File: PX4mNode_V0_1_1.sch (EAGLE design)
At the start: 128 parts, among them J201 DF13C-6P-1.25V, J202 DF13C-6P-1.25V, J203 DF13C-6P-1.25V, J301 DF13C-4P-1.25V, J401 DF13C-7P-1.25V, J402 DF13-4P-1.25V, J403 DF13C-4P-1.25V, J404 DF13C-4P-1.25V, J405 DF13C-4P-1.25V, J801 DF13C-3P-1.25V, M3_MOUNT1101 MOUNT-HOLE3.1MM, M3_MOUNT1102 MOUNT-HOLE3.1MM, M3_MOUNT1103 MOUNT-HOLE3.1MM, M3_MOUNT1104 MOUNT-HOLE3.1MM, U101 STM32F4X7VX, U401 MAX3051, U402 MAX3051, X101 3.2x2.5 mm / 24 MHz / 15 ppm

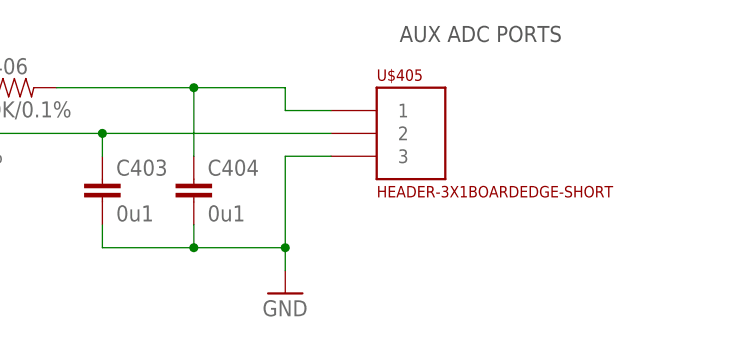
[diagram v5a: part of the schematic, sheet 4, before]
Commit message: Renamed and moved some component names
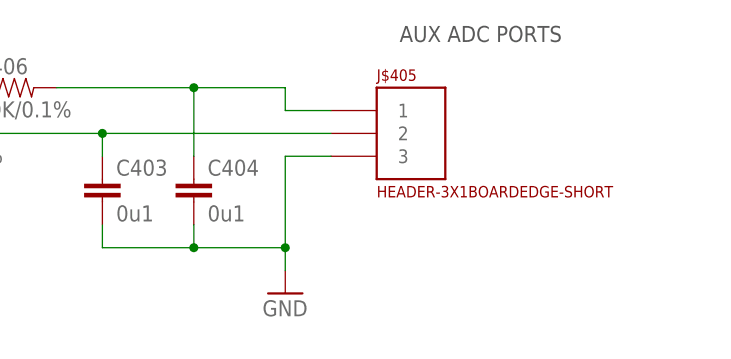
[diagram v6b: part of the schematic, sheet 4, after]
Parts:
- renumbered U$405 to J$405, U$601 to L$601
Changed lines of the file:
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@@
 <part name="L402" library="PX4lite" deviceset="NUF8402MN" device=""/>
 <part name="SJ403" library="SparkFun-Passives" deviceset="SOLDERJUMPER" device="TRACE"/>
-<part name="U$405" library="PX4lite" deviceset="HEADER-3X1" device="BOARDEDGE-SHORT"/>
+<part name="J$405" library="PX4lite" deviceset="HEADER-3X1" device="BOARDEDGE-SHORT"/>
 <part name="C403" library="pixhawk2" deviceset="CAP" device="0402" value="0u1">
 <attribute name="PARTNO" value="CC0402ZRY5V7BB104"/>
@@
 <part name="D903" library="SparkFun-DiscreteSemi" deviceset="DIODE" device="SMA" value="B340A"/>
 <part name="U$602" library="PX4lite" deviceset="TPS6303X" device=""/>
-<part name="U$601" library="ti_tps_soln2" deviceset="XFL4020-222MEB" device=""/>
+<part name="L$601" library="ti_tps_soln2" deviceset="XFL4020-222MEB" device=""/>
 <part name="SUPPLY2" library="supply2" deviceset="GND" device=""/>
 <part name="C607" library="SparkFun-Capacitors" deviceset="22UF-16V-20%-(1210)" device="" value="22uF"/>
@@
 <instance part="L402" gate="G$4" x="127" y="132.08"/>
 <instance part="SJ403" gate="1" x="205.74" y="58.42"/>
-<instance part="U$405" gate="G$1" x="228.6" y="157.48"/>
+<instance part="J$405" gate="G$1" x="228.6" y="157.48"/>
 <instance part="C403" gate="G$1" x="195.58" y="152.4">
 <attribute name="PARTNO" x="195.58" y="152.4" size="1.778" layer="96" display="off"/>
@@
 <wire x1="205.74" y1="165.1" x2="215.9" y2="165.1" width="0.1524" layer="91"/>
 <wire x1="215.9" y1="165.1" x2="215.9" y2="162.56" width="0.1524" layer="91"/>
-<pinref part="U$405" gate="G$1" pin="1"/>
+<pinref part="J$405" gate="G$1" pin="1"/>
 <wire x1="215.9" y1="162.56" x2="220.98" y2="162.56" width="0.1524" layer="91"/>
 <pinref part="C404" gate="G$1" pin="1"/>
@@
 <pinref part="R405" gate="G$1" pin="2"/>
 <wire x1="182.88" y1="160.02" x2="195.58" y2="160.02" width="0.1524" layer="91"/>
-<pinref part="U$405" gate="G$1" pin="2"/>
+<pinref part="J$405" gate="G$1" pin="2"/>
 <pinref part="C403" gate="G$1" pin="1"/>
 <wire x1="195.58" y1="160.02" x2="220.98" y2="160.02" width="0.1524" layer="91"/>
@@
 <wire x1="220.98" y1="157.48" x2="215.9" y2="157.48" width="0.1524" layer="91"/>
 <wire x1="215.9" y1="157.48" x2="215.9" y2="147.32" width="0.1524" layer="91"/>
-<pinref part="U$405" gate="G$1" pin="3"/>
+<pinref part="J$405" gate="G$1" pin="3"/>
 <pinref part="C403" gate="G$1" pin="2"/>
 <wire x1="215.9" y1="147.32" x2="215.9" y2="144.78" width="0.1524" layer="91"/>
@@
 <instance part="FRAME11" gate="G$1" x="0" y="0"/>
 <instance part="U$602" gate="A" x="101.6" y="109.22" smashed="yes"/>
-<instance part="U$601" gate="A" x="101.6" y="144.78" smashed="yes">
+<instance part="L$601" gate="A" x="101.6" y="144.78" smashed="yes">
 <attribute name="NAME" x="96.8756" y="149.4536" size="2.0828" layer="95" ratio="6" rot="SR0"/>
 <attribute name="VALUE" x="88.3158" y="141.1986" size="2.0828" layer="96" ratio="6" rot="SR0"/>
@@
 <wire x1="121.92" y1="129.54" x2="124.46" y2="129.54" width="0.1524" layer="91"/>
 <wire x1="124.46" y1="129.54" x2="124.46" y2="144.78" width="0.1524" layer="91"/>
-<pinref part="U$601" gate="A" pin="1"/>
+<pinref part="L$601" gate="A" pin="1"/>
 <wire x1="124.46" y1="144.78" x2="109.22" y2="144.78" width="0.1524" layer="91"/>
 </segment>
@@
 <net name="N$17" class="0">
 <segment>
-<pinref part="U$601" gate="A" pin="2"/>
+<pinref part="L$601" gate="A" pin="2"/>
 <wire x1="93.98" y1="144.78" x2="78.74" y2="144.78" width="0.1524" layer="91"/>
 <wire x1="78.74" y1="144.78" x2="78.74" y2="129.54" width="0.1524" layer="91"/>
